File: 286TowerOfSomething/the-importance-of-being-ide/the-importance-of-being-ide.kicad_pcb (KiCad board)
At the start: 2 copper layers, 70 parts, among them J1 Bus_ISA_16bit, J2 Conn_02x20_Odd_Even, J3 Conn_02x20_Odd_Even, J4 Conn_01x02, J5 Conn_01x02, J6 Conn_01x02, SW1 SW_DIP_x08, U1 SST39SF010, U10 74ALS125, U11 74ALS125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

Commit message: More layout work.
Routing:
- net /D15: track 150.5 -> 193.2 mm, vias 1 -> 5
- net /D14: track 146.0 -> 187.5 mm, vias 1 -> 5
- net /D13: track 141.6 -> 181.8 mm, vias 1 -> 5
- net /D12: track 137.2 -> 176.1 mm, vias 1 -> 5
- net /IDE2-D8: track 0.00 -> 38.9 mm
- net /IDE2-D15: track 0.00 -> 38.9 mm
- net /IDE2-D14: track 0.00 -> 38.9 mm
- net /IDE2-D9: track 0.00 -> 38.9 mm
- net /IDE2-D12: track 0.00 -> 38.9 mm
- net /IDE2-D11: track 0.00 -> 38.9 mm
- net /IDE2-D10: track 0.00 -> 38.9 mm
- net /IDE1-D9: track 0.00 -> 38.9 mm
- net /IDE1-D8: track 0.00 -> 38.9 mm
- net /IDE1-D15: track 0.00 -> 38.9 mm
- net /IDE1-D14: track 0.00 -> 38.9 mm
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
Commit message: Ripping up traces, I'm rethinking the layout
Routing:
- net /D6: track 201.7 -> 0.00 mm, vias 3 -> 0
- net /D5: track 196.0 -> 0.00 mm, vias 3 -> 0
- net /D15: track 193.2 -> 0.00 mm, vias 5 -> 0
- net /D4: track 190.3 -> 0.00 mm, vias 3 -> 0
- net /D14: track 187.5 -> 0.00 mm, vias 5 -> 0
- net /D3: track 184.6 -> 0.00 mm, vias 3 -> 0
- net /D13: track 181.8 -> 0.00 mm, vias 5 -> 0
- net /D2: track 178.8 -> 0.00 mm, vias 3 -> 0
- net /D12: track 176.1 -> 0.00 mm, vias 5 -> 0
- net /D1: track 173.1 -> 0.00 mm, vias 3 -> 0
- net /D11: track 170.4 -> 0.00 mm, vias 5 -> 0
- net /D0: track 167.4 -> 0.00 mm, vias 3 -> 0
- net /D10: track 164.7 -> 0.00 mm, vias 5 -> 0
- net /D7: track 163.2 -> 0.00 mm, vias 3 -> 0
- net /D9: track 158.9 -> 0.00 mm, vias 5 -> 0
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
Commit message: More work on layout of IDE card
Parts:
- J4: value Conn_01x02 -> IDE1_ACT
- J5: value Conn_01x02 -> IDE2_ACT
- J6: value Conn_01x02 -> IDE_ACT
- JP1: value Jumper_2_Open -> IDE1_PWR
- JP10: value Jumper_2_Open -> IDE2_IORDY
- JP2: value Jumper_2_Open -> IDE1_PU
- JP3: value Jumper_2_Open -> IDE2_PU
- JP4: value Jumper_2_Open -> IDE2_PWR
- JP5: value Jumper_3_Open -> IDE1_MODE
- JP6: value Jumper_3_Open -> IDE2_MODE
- JP7: value Jumper_3_Open -> IDE1_CSEL
- JP8: value Jumper_3_Open -> IDE2_CSEL
- JP9: value Jumper_2_Open -> IDE1_IORDY
- moved U14 206.7 mm to (57.1, 120.0), turned to 90 degrees
- moved C14 204.7 mm to (54.6, 116.2), turned to -90 degrees
- moved C12 204.2 mm to (52.1, 128.9), turned to -90 degrees
- moved C4 203.8 mm to (76.2, 128.9), turned to -90 degrees
- moved U8 203.5 mm to (54.6, 132.7), turned to 90 degrees
- moved U7 203.2 mm to (78.7, 132.7), turned to 90 degrees
- moved U12 195.9 mm to (120.7, 132.7), turned to 90 degrees
- moved U6 195.7 mm to (142.2, 132.7), turned to 90 degrees
- moved C3 194.1 mm to (118.1, 128.9), turned to -90 degrees
- moved C13 194.0 mm to (139.7, 128.9), turned to -90 degrees
- moved JP9 118.0 mm to (67.9, 91.4)
- moved JP7 105.7 mm to (59.1, 94.0), turned to 90 degrees
- moved JP5 98.8 mm to (59.0, 90.2), turned to 90 degrees
- moved JP8 98.6 mm to (122.6, 94.0), turned to 90 degrees
- moved JP6 97.0 mm to (122.6, 90.2), turned to 90 degrees
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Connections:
- JP10 pad 1: /IORDY -> /IDE2-IORDY
- JP10 pad 2: /IDE2-IORDY -> /IORDY
- U2 pad 19: /~{IDE1_LO} -> /~{IDE1-LO}
- U3 pad 19: /~{IDE1_HI} -> /~{IDE1-HI}
- U4 pad 19: /~{IDE2_LO} -> /~{IDE2-LO}
- U5 pad 19: /~{IDE2_HI} -> /~{IDE2-HI}
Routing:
- net /D7: track 0.00 -> 253.0 mm, vias 0 -> 10
- net /D3: track 0.00 -> 138.8 mm, vias 0 -> 4
- net /D4: track 0.00 -> 138.2 mm, vias 0 -> 4
- net /D5: track 0.00 -> 137.6 mm, vias 0 -> 4
- net /D6: track 0.00 -> 136.9 mm, vias 0 -> 4
- net /IOCS16: track 0.00 -> 127.2 mm, vias 0 -> 4
- net /D2: track 0.00 -> 125.5 mm, vias 0 -> 4
- net /D1: track 0.00 -> 119.8 mm, vias 0 -> 4
- net /D0: track 0.00 -> 114.1 mm, vias 0 -> 2
- net /~{0x376}: track 0.00 -> 105.9 mm, vias 0 -> 4
- net /~{0x170}: track 0.00 -> 102.2 mm, vias 0 -> 4
- net /~{IDE1-D7W}: track 0.00 -> 90.2 mm, vias 0 -> 4
- net /~{0x3F6}: track 0.00 -> 83.9 mm, vias 0 -> 4
- net /~{0x1F0}: track 0.00 -> 83.2 mm, vias 0 -> 4
- net /~{IDE1-D7R}: track 0.00 -> 82.6 mm, vias 0 -> 4
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
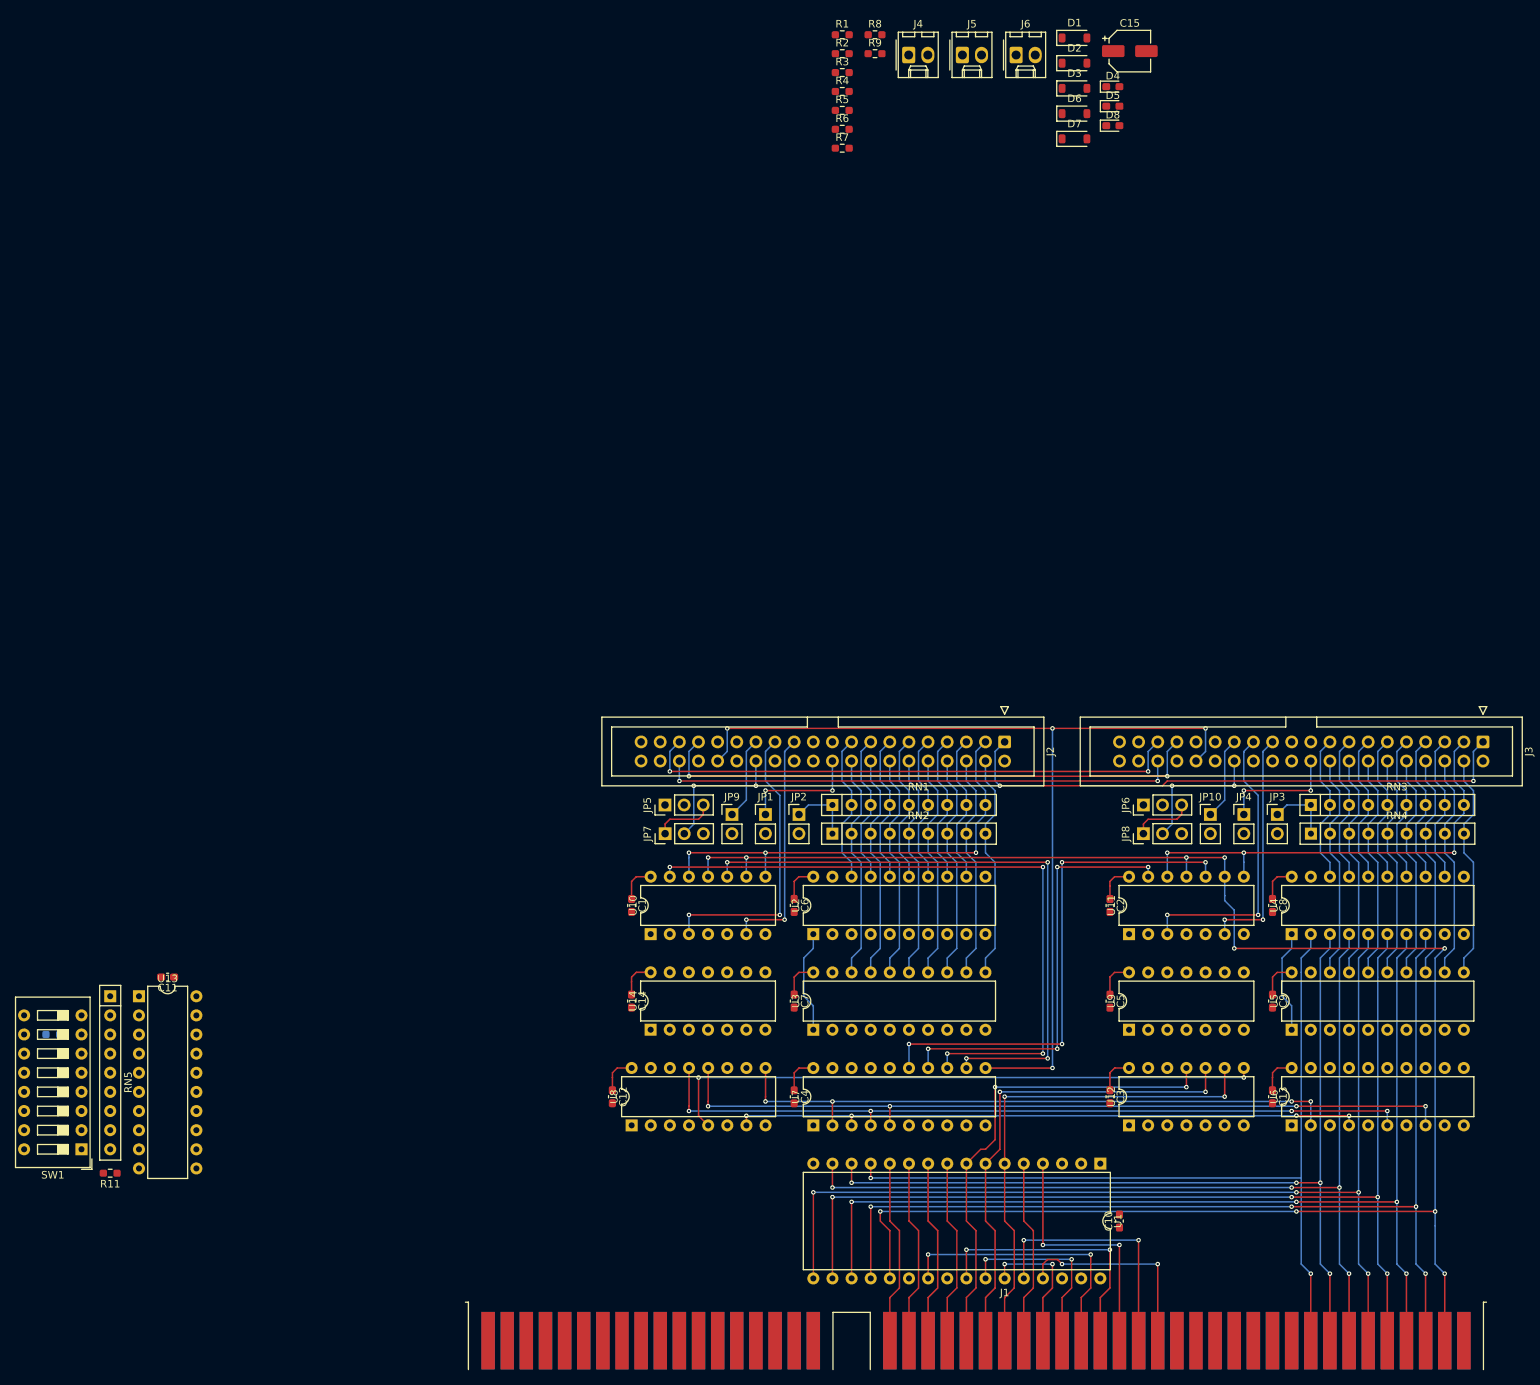
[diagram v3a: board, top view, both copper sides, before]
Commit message: Schematic corrections, and layout almost done
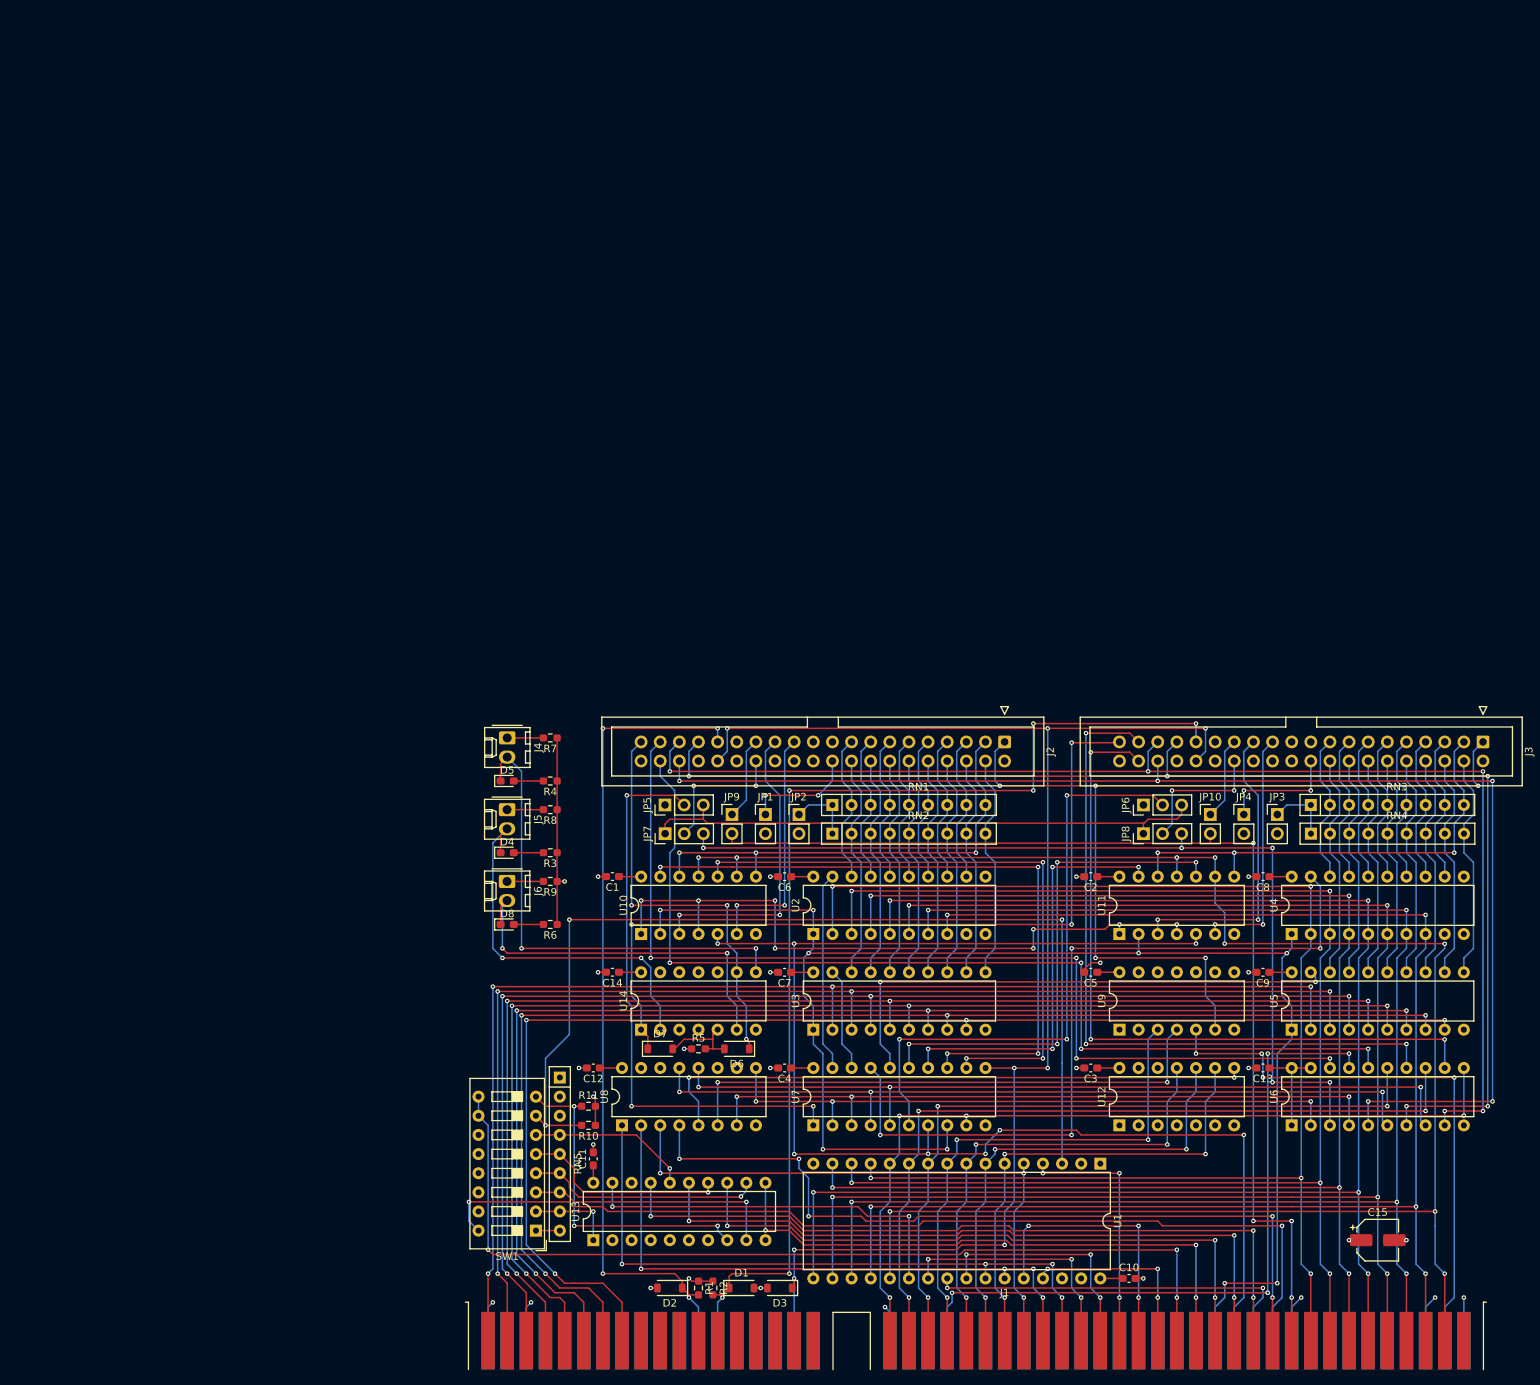
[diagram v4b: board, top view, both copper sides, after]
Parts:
- R10: moved to F.Cu
- moved D1 171.7 mm to (69.2, 154.3)
- moved D2 171.3 mm to (59.7, 154.3), turned to 180 degrees
- moved R1 167.5 mm to (63.5, 154.3), turned to -90 degrees
- moved R2 164.8 mm to (65.4, 154.3), turned to -90 degrees
- moved D3 164.0 mm to (74.3, 154.3), turned to 180 degrees
- moved C15 161.2 mm to (153.7, 148.0)
- moved D8 133.1 mm to (38.1, 106.0)
- moved D7 132.7 mm to (58.4, 122.6)
- moved D6 132.0 mm to (68.6, 122.6), turned to 180 degrees
- moved D4 129.6 mm to (38.1, 96.5)
- moved J6 128.9 mm to (38.1, 100.3), turned to -90 degrees
- moved R5 126.0 mm to (63.5, 122.6)
- moved D5 120.4 mm to (38.1, 87.0)
- moved R9 118.0 mm to (43.8, 100.3), turned to 180 degrees
- moved J5 117.0 mm to (38.1, 90.8), turned to -90 degrees
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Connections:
- U6 pad 10: Net-(U6-GND) -> GND
- U7 pad 10: Net-(U6-GND) -> GND
- U9 pad 3: (no net) -> /A3
- U9 pad 4: (no net) -> /~{A3}
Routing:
- net /IOW: track 0.00 -> 187.6 mm, vias 0 -> 8
- net /IOR: track 27.5 -> 205.9 mm, vias 0 -> 9
- net /D8: track 0.00 -> 175.2 mm, vias 0 -> 4
- net /D9: track 0.00 -> 173.7 mm, vias 0 -> 4
- net /D10: track 0.00 -> 172.2 mm, vias 0 -> 4
- net /D11: track 0.00 -> 170.6 mm, vias 0 -> 4
- net /D12: track 0.00 -> 169.1 mm, vias 0 -> 4
- net /D13: track 0.00 -> 168.3 mm, vias 0 -> 4
- net /D14: track 0.00 -> 167.5 mm, vias 0 -> 4
- net /D15: track 0.00 -> 167.3 mm, vias 0 -> 4
- net /IRQ15: track 0.00 -> 148.1 mm, vias 0 -> 6
- net /IORDY: track 0.00 -> 142.9 mm, vias 0 -> 4
- net /~{CS3FX}: track 0.00 -> 134.5 mm, vias 0 -> 4
- net /~{CS1FX}: track 0.00 -> 134.0 mm, vias 0 -> 4
- net /FLASH_A15: track 0.00 -> 133.0 mm, vias 0 -> 3
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- added copper zone on In1.Cu, net +5V
- added copper zone on In2.Cu, net GND
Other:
- copper layers 2 -> 4

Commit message: Last trace put in
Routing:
- net /~{ROMWE}: track 3.18 -> 84.4 mm, vias 0 -> 2

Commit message: Adding bracket to The Importance of Being IDE
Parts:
- added BRACKET1: ~, pc-parts:PC_BRACKET_ISA_KEYSTONE_9202_Rev1, F.Cu at (190.5, 126.4)
- moved C15 46.3 mm to (179.1, 109.2)
- moved D2 46.3 mm to (85.1, 115.6)
- moved D6 46.3 mm to (94.0, 83.8)
- moved R1 46.3 mm to (88.9, 115.6)
- moved R2 46.3 mm to (90.8, 115.6)
- moved R5 46.3 mm to (88.9, 83.8)
- moved U13 46.3 mm to (74.9, 109.2)
- moved C10 46.3 mm to (146.1, 114.3)
- moved C11 46.3 mm to (74.9, 98.4)
- moved C12 46.3 mm to (74.9, 86.4)
- moved C13 46.3 mm to (163.8, 86.4)
- moved C3 46.3 mm to (141.0, 86.4)
- moved C5 46.3 mm to (141.0, 73.7)
- moved C9 46.3 mm to (163.8, 73.7)
- moved D1 46.3 mm to (94.6, 115.6)
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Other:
- board outline added: 165.4 x 88.9 mm
- board text added: "COMBINED ACTIVITY"
- board text added: "COM_A15"
- board text added: "CSEL"
- board text added: "FLSH_A15"
- board text added: "IDE_EN"
- board text added: "IORDY"
- board text added: "PRIMARY"
- board text added: "PRIMARY ACTIVITY"
- board text added: "PU"
- board text added: "PWR"
- board text added: "ROM_A15"
- board text added: "ROM_A16"
- board text added: "ROM_A17"
- board text added: "ROM_A18"
- board text added: "ROM_EN"
- board text added: "ROM_WR"
- board text added: "SECONDARY"
- board text added: "SECONDARY ACTIVITY"
- board text added: "The Importance of Being IDE 2025-01-04 by rglenn"
